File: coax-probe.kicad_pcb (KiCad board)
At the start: 2 copper layers, 27 x 10 mm, 28 parts, among them J1 Conn_01x02, J2 Conn_Coaxial, J3 Conn_01x02, J4 Conn_01x03, J5 Conn_Coaxial, J6 Conn_01x03, U1 THS3001, U2 INA128, U3 THS3001

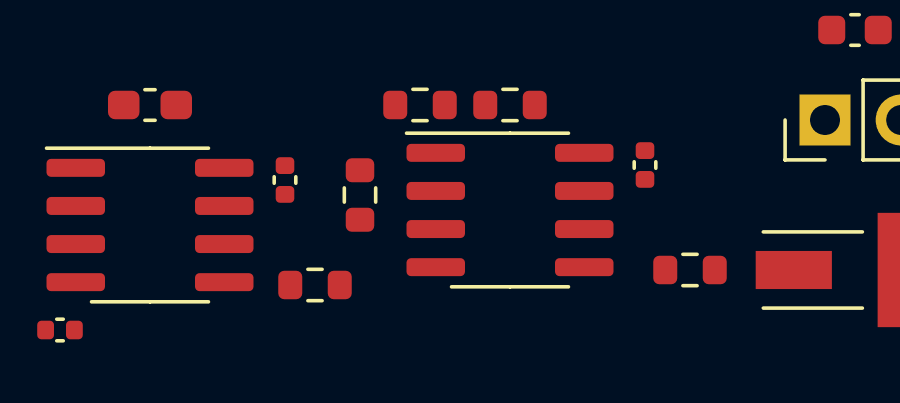
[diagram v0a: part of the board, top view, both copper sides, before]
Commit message: use dual-supply for differential amp buffer
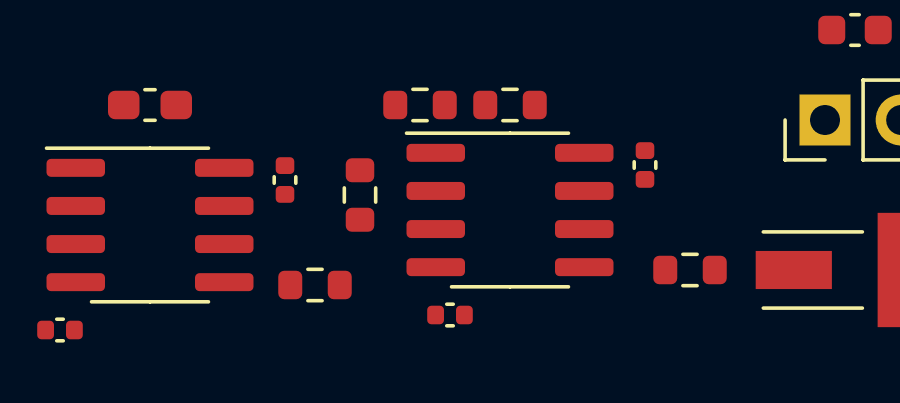
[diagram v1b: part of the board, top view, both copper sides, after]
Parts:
- added C8: 100nF, Capacitor_SMD:C_0402_1005Metric, F.Cu at (164.0, 82.0)
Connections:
- U3 pad 4: GND -> VSS

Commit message: Improvements, layout
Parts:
- removed C2, C7: 10uF, Capacitor_SMD:C_0603_1608Metric
- removed C4, C8: 100nF, Capacitor_SMD:C_0402_1005Metric
- removed D1, D2: SM4007PL, Diode_SMD:D_SOD-123F
- added C10: 10uF, Capacitor_SMD:C_0603_1608Metric, F.Cu at (174.9, 67.7)
- added C11: 10uF, Capacitor_SMD:C_0603_1608Metric, F.Cu at (174.1, 64.7)
- added C13: 100nF, Capacitor_SMD:C_0402_1005Metric, F.Cu at (157.5, 79.3)
- added C9: 100nF, Capacitor_SMD:C_0402_1005Metric, F.Cu at (167.4, 62.1)
- added R11: 0, Resistor_SMD:R_0603_1608Metric, F.Cu at (173.4, 78.2)
- added R12: -, Resistor_SMD:R_0603_1608Metric, F.Cu at (175.0, 78.2)
- added U4: CJ431, Package_TO_SOT_SMD:SOT-23, F.Cu at (170.9, 78.3)
- J3: value Conn_01x02 -> Conn_01x03; footprint Connector_PinHeader_2.54mm:PinHeader_1x02_P2.54mm_Vertical -> Connector_PinHeader_2.54mm:PinHeader_1x03_P2.54mm_Vertical
- J6: value Conn_01x03 -> Conn_01x02; footprint Connector_PinHeader_2.54mm:PinHeader_1x03_P2.54mm_Vertical -> Connector_PinHeader_2.54mm:PinHeader_1x02_P2.54mm_Vertical
- R1: value 750 -> 175
- R2, R3, R8, R9: value 750 -> 402
- R5: value RG -> -
- R6: value 0 -> 175
- R7: value 10k -> 175
- U1, U3: value THS3001 -> OPA690; footprint Package_SO:SOIC-8_3.9x4.9mm_P1.27mm -> Package_TO_SOT_SMD:TSOT-23-6
- moved R10 11.7 mm to (162.9, 73.1)
- moved J3 7.86 mm to (177.8, 68.2)
- moved R7 7.22 mm to (168.2, 77.4), turned to 270 degrees
- moved J5 7.15 mm to (175.8, 73.7)
- moved R4 6.80 mm to (170.1, 61.9), turned to 180 degrees
- moved C6 6.22 mm to (178.0, 78.7), turned to 270 degrees
- moved C5 5.77 mm to (165.3, 74.5)
- moved J6 5.52 mm to (180.6, 79.2)
- moved J2 4.92 mm to (175.9, 62.4)
- moved R1 4.54 mm to (165.1, 63.7), turned to 180 degrees
- moved R8 4.33 mm to (166.6, 77.4), turned to 90 degrees
- moved J1 4.12 mm to (161.8, 63.7), turned to 0 degrees
- moved R6 3.67 mm to (160.2, 77.4), turned to 90 degrees
- moved J4 3.45 mm to (149.2, 78.5)
- moved U2 3.26 mm to (155.5, 76.1)
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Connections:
- J3 pad 2: GND -> VSS
- J4 pad 2: GND -> /IN-
- J4 pad 3: /IN- -> GND
- R6 pad 1: /Ref -> Net-(R6-Pad1)
- R6 pad 2: GND -> /INA
- R7 pad 1: /INA -> VCC
- R7 pad 2: GND -> REF
- U1 pad 1: (no net) -> Net-(R3-Pad1)
- U1 pad 2: Net-(R2-Pad1) -> VSS
- U1 pad 4: GND -> Net-(R2-Pad1)
- U1 pad 6: Net-(R3-Pad1) -> VCC
- U2 pad 4: VSS -> GND
- U2 pad 5: /Ref -> REF
- U3 pad 1: (no net) -> Net-(R10-Pad2)
- U3 pad 2: Net-(R8-Pad1) -> GND
- U3 pad 3: /INA -> Net-(R6-Pad1)
- U3 pad 4: VSS -> Net-(R8-Pad1)
- U3 pad 6: Net-(R10-Pad2) -> VCC
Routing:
- net VCC: track 13.6 -> 61.7 mm
- net VSS: track 0.00 -> 21.0 mm
- net REF: track 0.00 -> 17.5 mm
- net Net-(J5-Pad1): track 0.00 -> 9.78 mm
- net Net-(R8-Pad1): track 0.00 -> 6.13 mm
- net /IN+: track 0.00 -> 4.26 mm
- net Net-(R3-Pad1): track 7.52 -> 3.44 mm
- net Net-(R11-Pad2): track 0.00 -> 3.91 mm
- net /IN-: track 0.00 -> 3.73 mm
- net Net-(R10-Pad2): track 0.00 -> 3.44 mm
- net Net-(R5-Pad2): track 0.00 -> 3.13 mm
- net Net-(R5-Pad1): track 0.00 -> 3.13 mm
- net /INA: track 0.00 -> 2.19 mm
- net Net-(R6-Pad1): track 0.00 -> 2.12 mm
- net Net-(R1-Pad1): track 3.32 -> 1.43 mm
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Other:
- board size 27 x 10 mm -> 37.3 x 21 mm
- board text removed: "Active Probe 2x Gain"

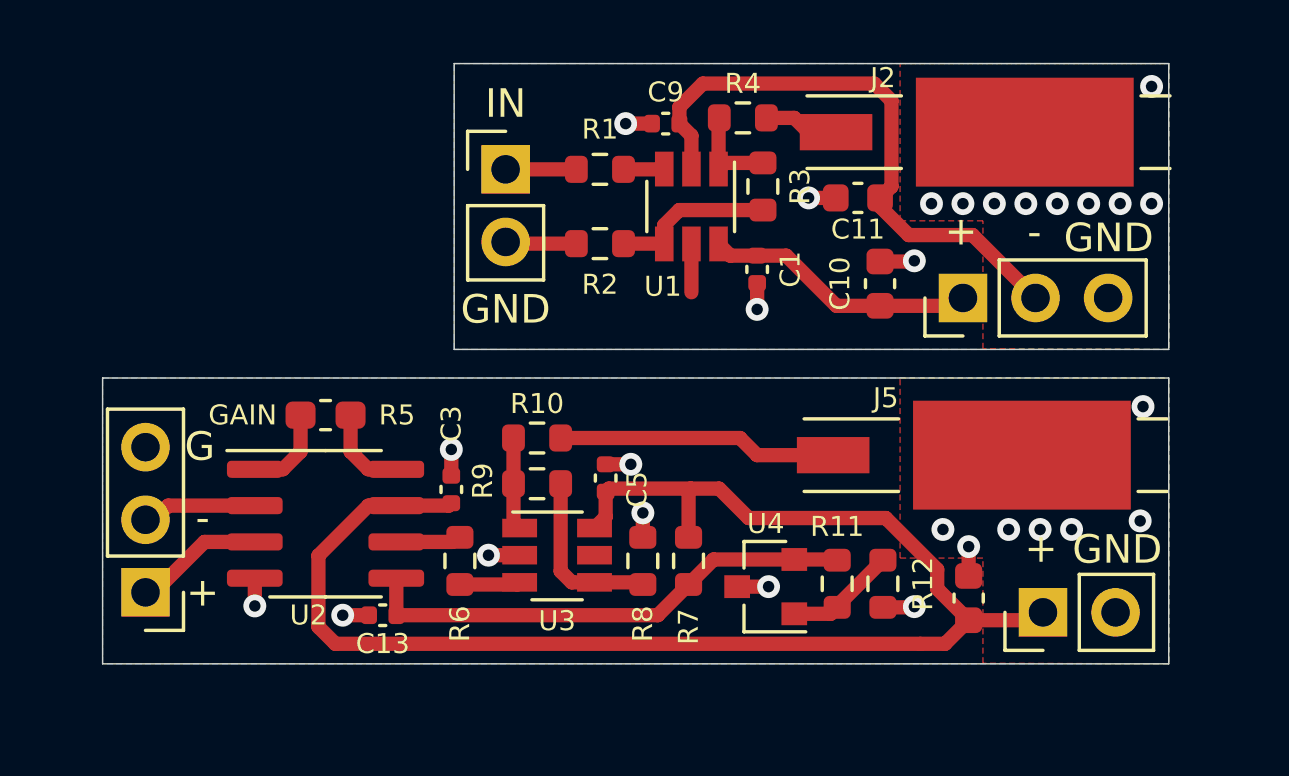
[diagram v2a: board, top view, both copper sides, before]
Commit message: Add charge pump. Improve layout.
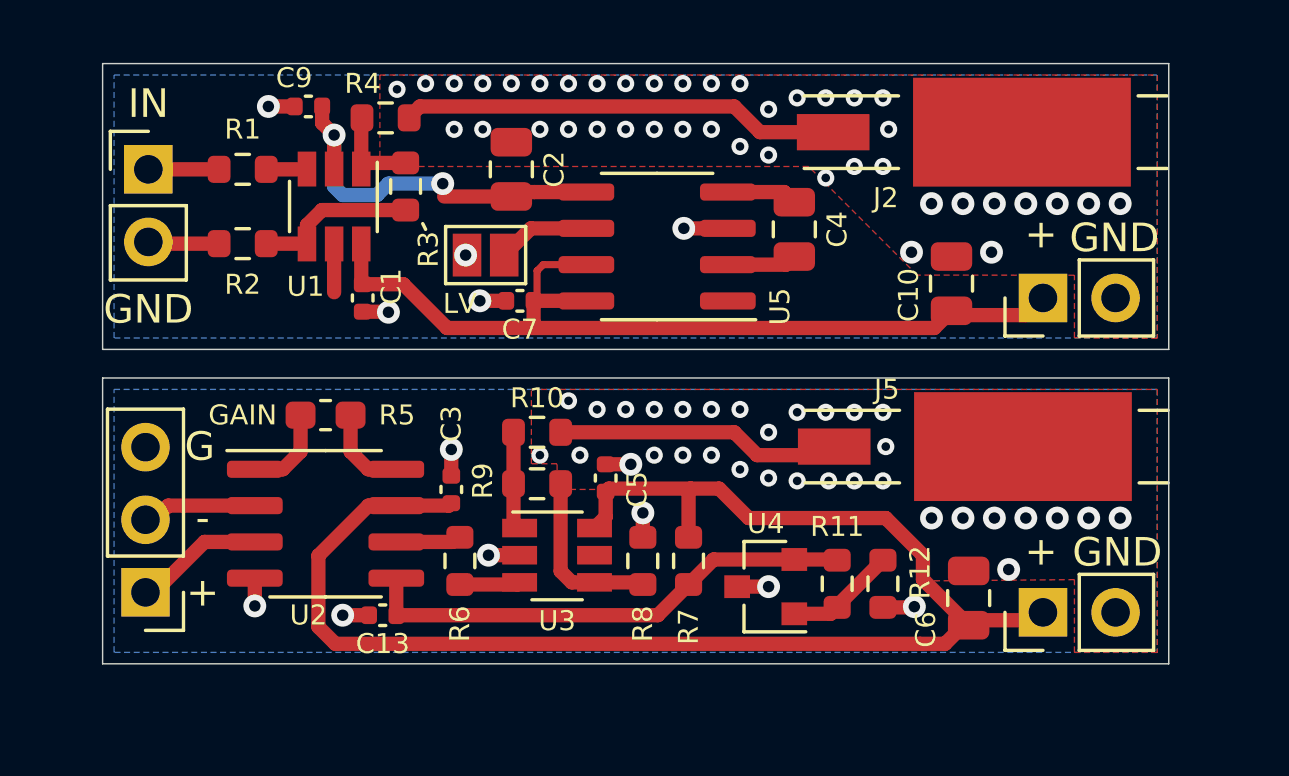
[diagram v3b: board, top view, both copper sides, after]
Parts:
- removed C11: 10uF, Capacitor_SMD:C_0603_1608Metric
- added C2: 10uF, Capacitor_SMD:C_0805_2012Metric, F.Cu at (162.0, 63.7)
- added C4: 10uF, Capacitor_SMD:C_0805_2012Metric, F.Cu at (171.9, 65.8)
- added C7: 100nF, Capacitor_SMD:C_0402_1005Metric, F.Cu at (162.3, 68.3)
- added JP1: LV, Jumper:SolderJumper-2_P1.3mm_Open_Pad1.0x1.5mm, F.Cu at (161.1, 66.7)
- added U5: ICL7660, Package_SO:SOIC-8_3.9x4.9mm_P1.27mm, F.Cu at (167.1, 66.4)
- C10, C6: footprint Capacitor_SMD:C_0603_1608Metric -> Capacitor_SMD:C_0805_2012Metric
- J3: value Conn_01x03 -> Conn_01x02; footprint Connector_PinHeader_2.54mm:PinHeader_1x03_P2.54mm_Vertical -> Connector_PinHeader_2.54mm:PinHeader_1x02_P2.54mm_Vertical
- moved C1 13.8 mm to (156.8, 68.2)
- moved C9 12.5 mm to (154.9, 61.5)
- moved J1 12.5 mm to (149.3, 63.7)
- moved R1 12.5 mm to (152.6, 63.7)
- moved R2 12.5 mm to (152.6, 66.3)
- moved R3 12.5 mm to (158.3, 64.3)
- moved R4 12.5 mm to (157.6, 61.9)
- moved U1 12.5 mm to (155.8, 65.0)
- moved J3 2.80 mm to (180.6, 68.2)
- moved C10 2.50 mm to (177.4, 67.7)
- moved J5 0.30 mm to (175.8, 73.4)
- moved R10 0.20 mm to (162.9, 72.9)
- moved J2 0.10 mm to (175.8, 62.4)
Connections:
- net Net-(J2-Pad1) renamed /OUT
- net Net-(J5-Pad1) renamed /OUTD
- J3 pad 2: VSS -> GND
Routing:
- net VCC: track 61.7 -> 84.4 mm
- net /OUT: track 2.64 -> 15.5 mm
- net VSS: track 21.0 -> 13.3 mm, vias 0 -> 2
- net Net-(JP1-Pad1): track 0.00 -> 3.26 mm
- net Net-(C4-Pad2): track 0.00 -> 2.47 mm
- net Net-(C4-Pad1): track 0.00 -> 2.44 mm
- net GND: track 15.4 -> 14.6 mm, vias 28 -> 87
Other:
- outline, holes or cut-outs redrawn
- net class 50 Ohm added: clearance 0.127, trace_width 0.65, via_dia 0.8, via_drill 0.4
- rule trace_min: 0.2 -> 0.127
- rule via_min_size: 0.4 -> 0.6
- board text added: "1.2MHz (G=1) 50Ω Active Differential Probe"
- board text added: "2.5V−6V"
- board text added: "220MHz 50Ω Active Probe"
- board text added: "5V−12V"
- board text added: "Gain=1+(50kΩ/RG) ICM: -2V−VCC+2V MAX: ±40V to GND"
- board text added: "Solder LV for <3V"
- board text added: "±3.3V input with 5V VCC MAX VCC+5V VSS-5V"
